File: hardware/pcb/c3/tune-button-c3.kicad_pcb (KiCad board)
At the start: 2 copper layers, 46 x 69.5 mm, 40 parts, among them J1 USB-C, J2 LiPo, Q1 AO3401A, SW1 MX switch, SW2 MX switch, SW3 MX switch, SW4 MX switch, SW5 RESET, SW6 BOOT, U1 ESP32-C3-WROOM-02-N4, U2 SRV05-4, U3 TP4054, U4 RT9080-3.3

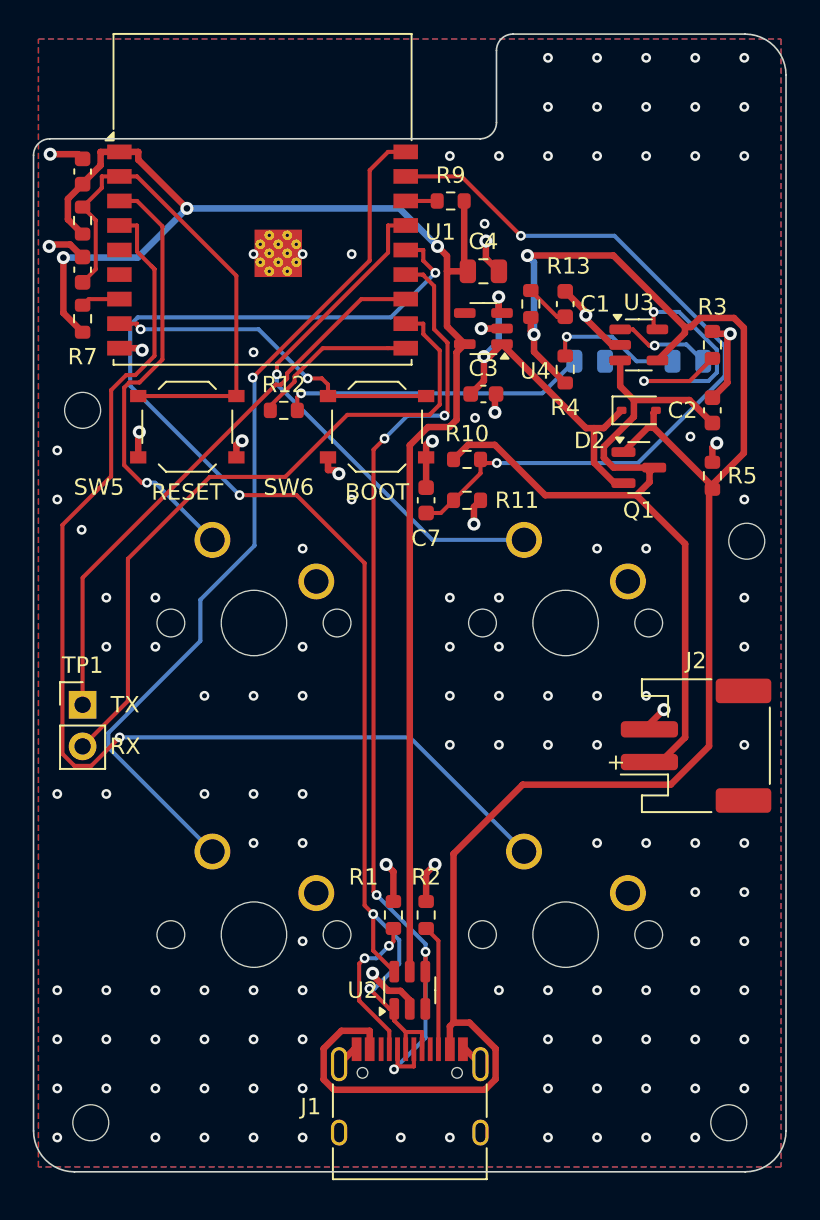
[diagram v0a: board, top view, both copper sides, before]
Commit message: pcb: fixes from the second DFM audit and visual review
- JLC BOM: no designator ranges (KiCad wrote R5-R7, so the CPL lost R5/R6/R7); fab_jlc.py now
  refuses a BOM part with no placement.
- Stitching vias kept off SMD pad openings (two were in the module ground pad's paste).
- Logo drawn as rows at the stroke pitch with caps inset, so gaps keep their size; 15 mm wide.
- Labels only where their own part is the nearest body (R13 and U4 were ambiguous).
- Battery + marks off the pads; USB-C slot paste overprinted 0.2 mm; footprint silk >= 0.15 mm.
- C3 board 70.1 mm long so the USB-C legs clear the switch housings by 0.3 mm.
- Stop tracking __pycache__.
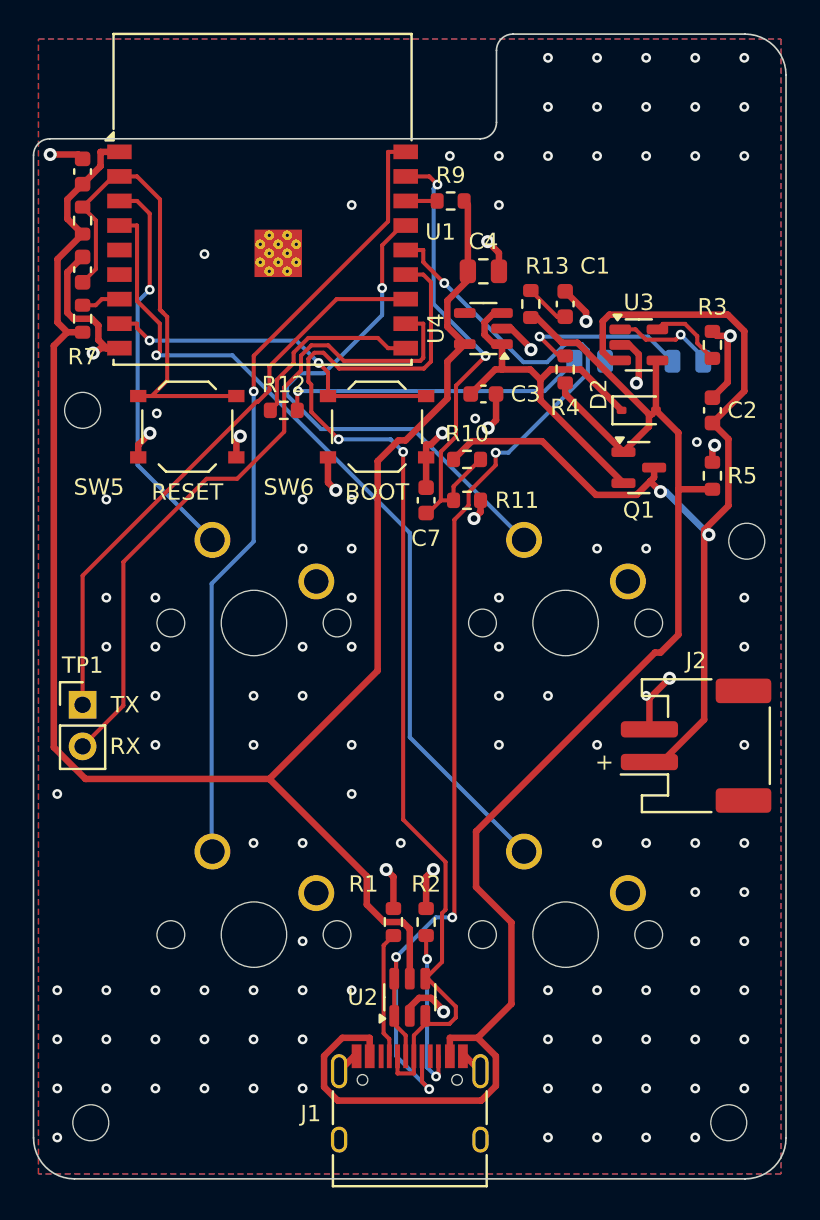
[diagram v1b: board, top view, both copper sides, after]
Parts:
- moved J1 0.43 mm to (23.0, 66.5)
- moved R1 0.43 mm to (22.0, 54.3)
- moved R2 0.43 mm to (24.0, 54.3)
- moved U2 0.43 mm to (23.0, 58.9)
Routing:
- net VBUS: track 116.0 -> 93.7 mm, vias 2 -> 0
- net VBAT_SENSE: track 48.0 -> 29.2 mm
- net K3: track 68.9 -> 52.1 mm
- net 3V3: track 96.2 -> 112.9 mm, vias 3 -> 0
- net VBAT: track 49.4 -> 62.8 mm, vias 0 -> 2
- net PROG: track 16.8 -> 4.63 mm, vias 2 -> 0
- net GND: track 44.8 -> 56.6 mm, vias 135 -> 124
- net USB_DP: track 84.0 -> 75.5 mm, vias 4 -> 5
- net USB_DN: track 62.5 -> 69.6 mm, vias 5 -> 2
- net K4: track 53.6 -> 48.3 mm
- net CHG_A: track 8.30 -> 10.8 mm
- net CC2: track 7.69 -> 10.2 mm, vias 0 -> 2
- net K2: track 26.5 -> 24.3 mm
- net CC1: track 9.45 -> 7.77 mm, vias 2 -> 0
- net EN: track 31.7 -> 30.2 mm
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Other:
- board size 46 x 69.5 mm -> 46 x 70 mm

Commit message: pcb (c3): fixes from the second simulation pass
- C1 4.7u -> 10u 0805 (C15850, Basic): with R13, plug-in ringing on low-resistance cables peaks
  around 5.6 V instead of 6.1 V (RT9080 absolute max 6.5 V).
- D4, a 1N5819WS across Q1: in the ~3-5 ms after unplugging, before Q1 turns on, the cell feeds
  VSYS through 0.35 V rather than the body diode's 0.6 V, so a Wi-Fi burst there stays above
  brown-out at a 3.4 V cell.
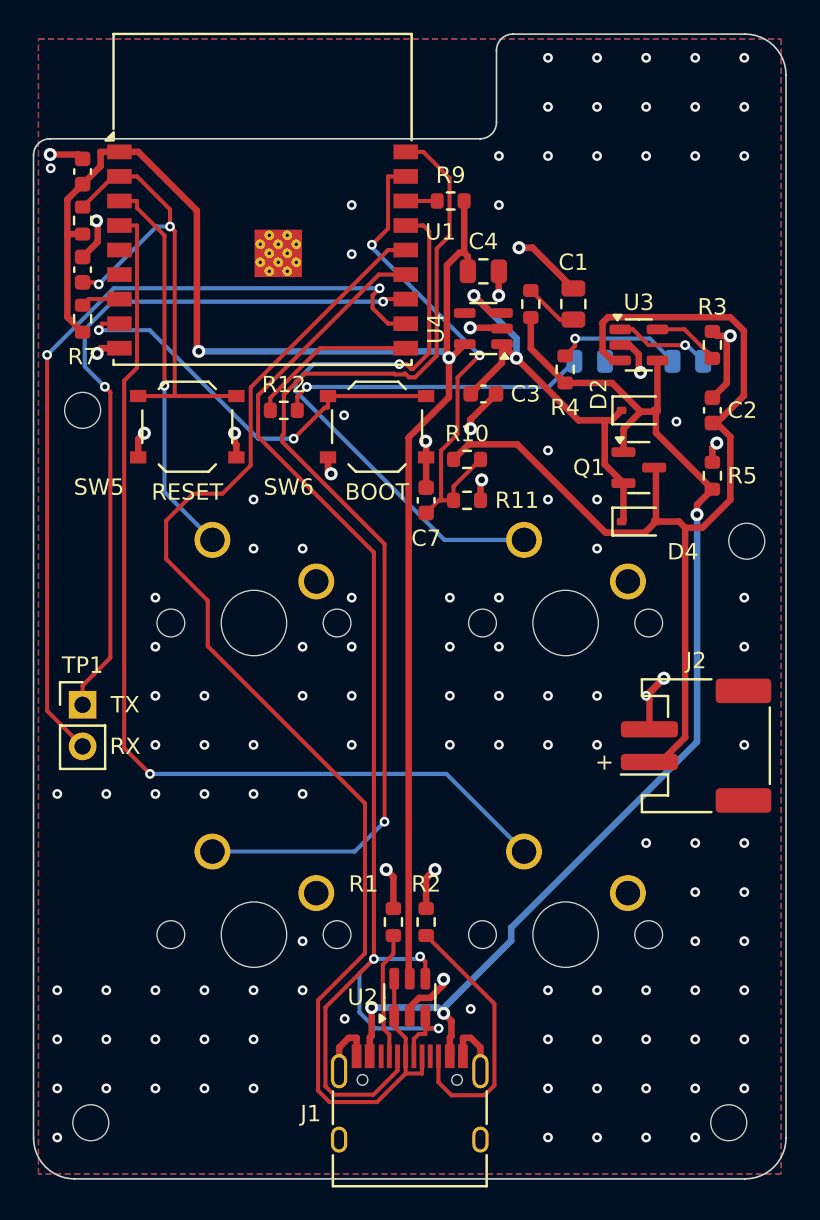
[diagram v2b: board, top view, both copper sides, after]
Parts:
- added D4: 1N5819WS, Diode_SMD:D_SOD-323, F.Cu at (37.0, 29.8)
- C1: value 4.7u -> 10u; footprint Capacitor_SMD:C_0603_1608Metric -> Capacitor_SMD:C_0805_2012Metric
- moved C1 0.50 mm to (33.0, 16.5)
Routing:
- net VBUS: track 93.7 -> 72.6 mm, vias 0 -> 3
- net K4: track 48.3 -> 65.1 mm
- net 3V3: track 112.9 -> 96.5 mm, vias 0 -> 2
- net USB_DN: track 69.6 -> 81.8 mm, vias 2 -> 3
- net TXD: track 35.5 -> 44.7 mm, vias 0 -> 2
- net RXD: track 41.9 -> 50.6 mm, vias 0 -> 2
- net K3: track 52.1 -> 60.4 mm
- net CC2: track 10.2 -> 16.5 mm, vias 2 -> 0
- net GND: track 56.6 -> 62.2 mm, vias 124 -> 129
- net USB_DP: track 75.5 -> 79.9 mm, vias 5 -> 0
- net IO9: track 21.6 -> 25.8 mm
- net K1: track 32.5 -> 36.4 mm
- net CHG_A: track 10.8 -> 7.84 mm
- net VSYS: track 24.7 -> 27.1 mm, vias 0 -> 2
- net LED: track 11.6 -> 10.3 mm
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
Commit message: pcb: black solder mask, white legend in the board stackup
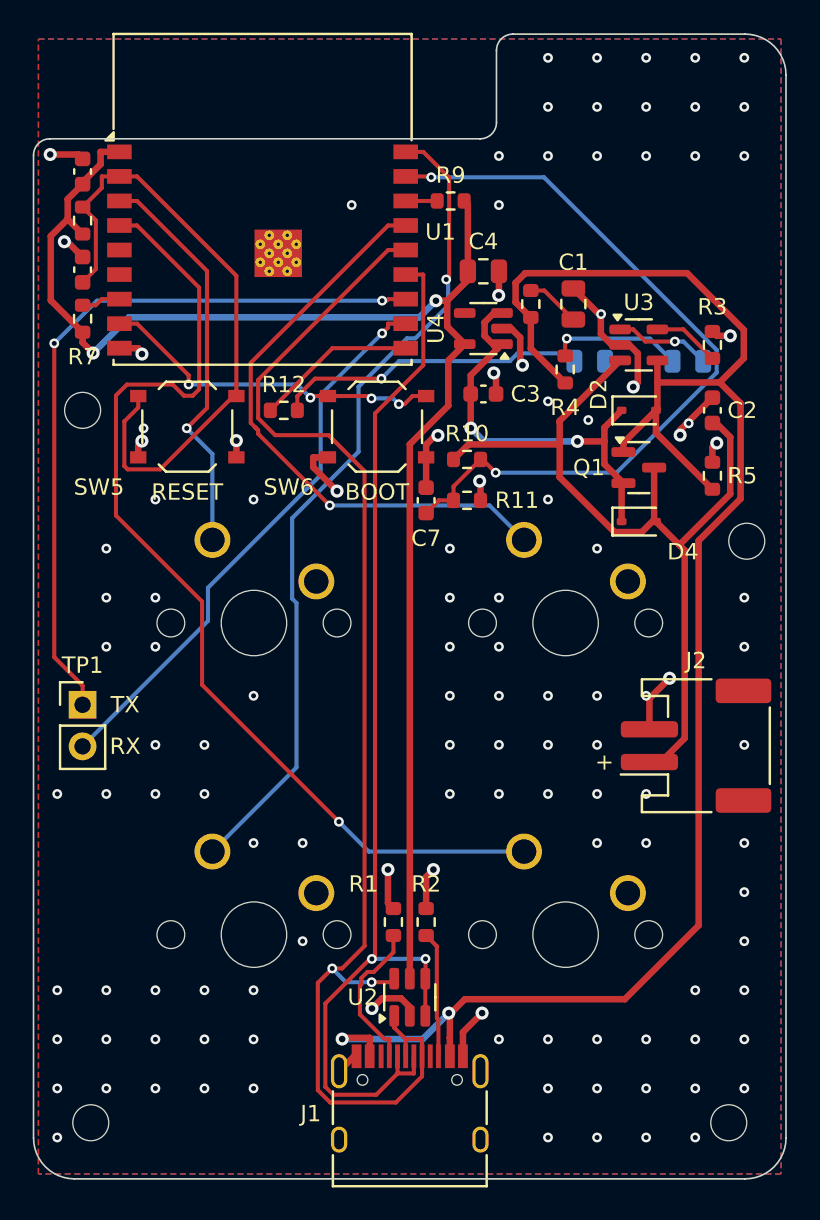
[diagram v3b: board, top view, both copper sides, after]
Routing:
- net VBUS: track 72.6 -> 108.5 mm, vias 3 -> 2
- net VBAT_SENSE: track 30.2 -> 47.3 mm
- net RXD: track 50.6 -> 34.7 mm, vias 2 -> 1
- net K4: track 65.1 -> 51.1 mm
- net USB_DN: track 81.8 -> 68.3 mm, vias 3 -> 2
- net VBAT: track 63.4 -> 52.4 mm
- net GND: track 62.2 -> 52.7 mm, vias 129 -> 122
- net CC2: track 16.5 -> 7.69 mm
- net EN: track 31.3 -> 39.4 mm, vias 2 -> 0
- net 3V3: track 96.5 -> 90.0 mm
- net IO9: track 25.8 -> 21.4 mm, vias 2 -> 4
- net K3: track 60.4 -> 62.2 mm
- net VSYS: track 27.1 -> 25.4 mm
- net CC1: track 7.81 -> 9.38 mm
- net K2: track 23.7 -> 24.7 mm
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
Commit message: pcb: third DFM audit and visual fixes
- JLCJLCJLCJLC order-number marker (C3 electronics side, XIAO back); README: black mask,
  lead-free HASL, 'Specify a location', overhang remark.
- Logo scaled by the mark's own extent (15 mm printed, was 12.4); vias 1 mm clear of back art.
- D1/D3 labels merged into the back text; keycaps are label obstacles on front-key boards.
- USB-C slot paste overprint 0.12 mm (0.15 mm stencil web).
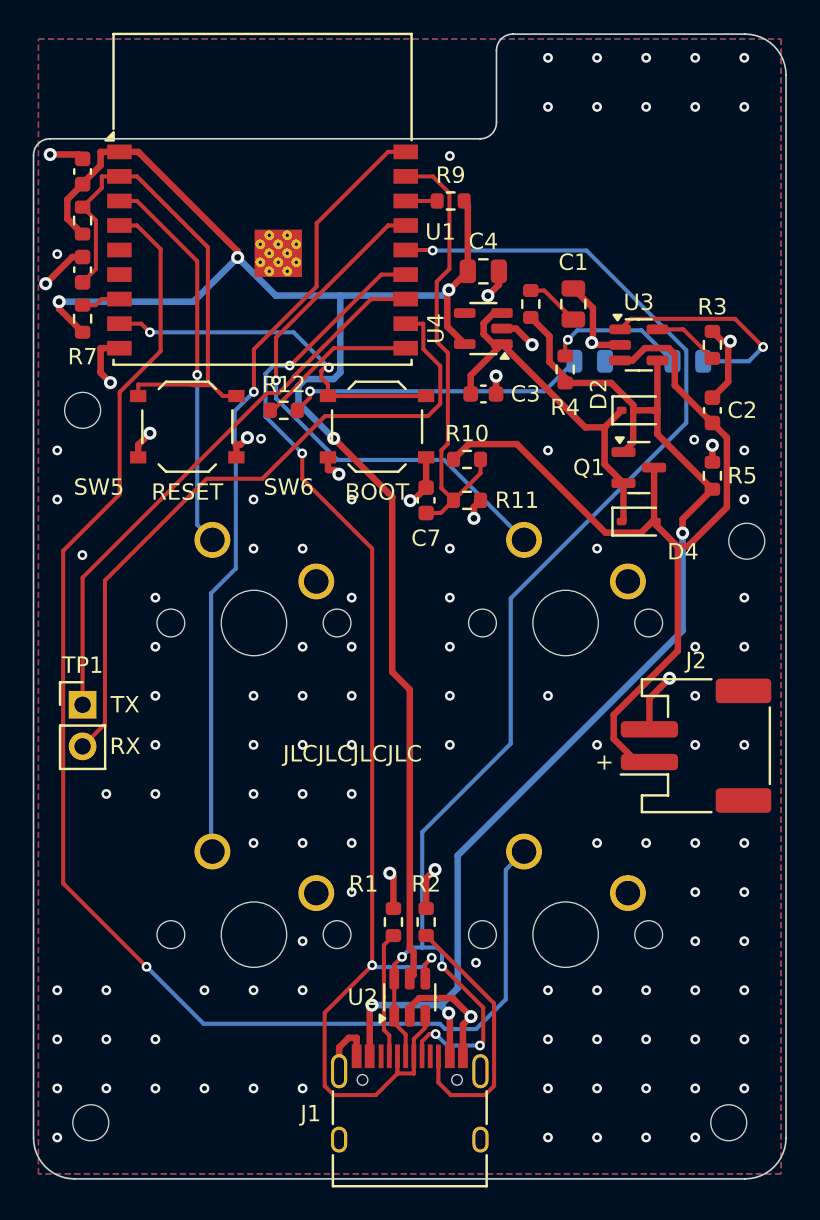
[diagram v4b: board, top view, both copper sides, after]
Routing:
- net VBUS: track 108.5 -> 72.8 mm, vias 2 -> 3
- net K3: track 62.2 -> 85.4 mm
- net VBAT_SENSE: track 47.3 -> 28.1 mm, vias 2 -> 0
- net 3V3: track 90.0 -> 102.7 mm, vias 2 -> 4
- net TXD: track 45.4 -> 34.6 mm, vias 2 -> 0
- net CC2: track 7.69 -> 16.5 mm
- net EN: track 39.4 -> 31.3 mm
- net STAT: track 5.88 -> 13.7 mm
- net RXD: track 34.7 -> 42.1 mm, vias 1 -> 0
- net USB_DN: track 68.3 -> 75.0 mm, vias 2 -> 4
- net USB_DP: track 79.5 -> 84.0 mm, vias 2 -> 5
- net VBAT: track 52.4 -> 55.3 mm
- net K1: track 36.7 -> 33.9 mm
- net K4: track 51.1 -> 48.4 mm
- net GND: track 52.7 -> 55.4 mm
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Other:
- board text added: "D1 CHG"
- board text added: "D3 LED"
- board text added: "JLCJLCJLCJLC"
- board text removed: "CHG"
- board text removed: "LED"

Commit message: pcb (c3): fixes from the third simulation pass
- C1's damping resistor 1 -> 0.5 ohm (R13 + R14, two Basic 1 ohm): with 1 ohm a stiff 5.5 V
  source and no cell rang VSYS to 6.8 V, past the RT9080's 6.5 V; 0.47 ohm simulated under 6.4 V
  on every cable corner.
- R5 10k -> 3.3k: the bigger C1 had stretched the unplug gap to 13-28 ms; ~5-7 ms again.
- README: D4's hot reverse leakage means the cell's protection board is the overcharge backstop.
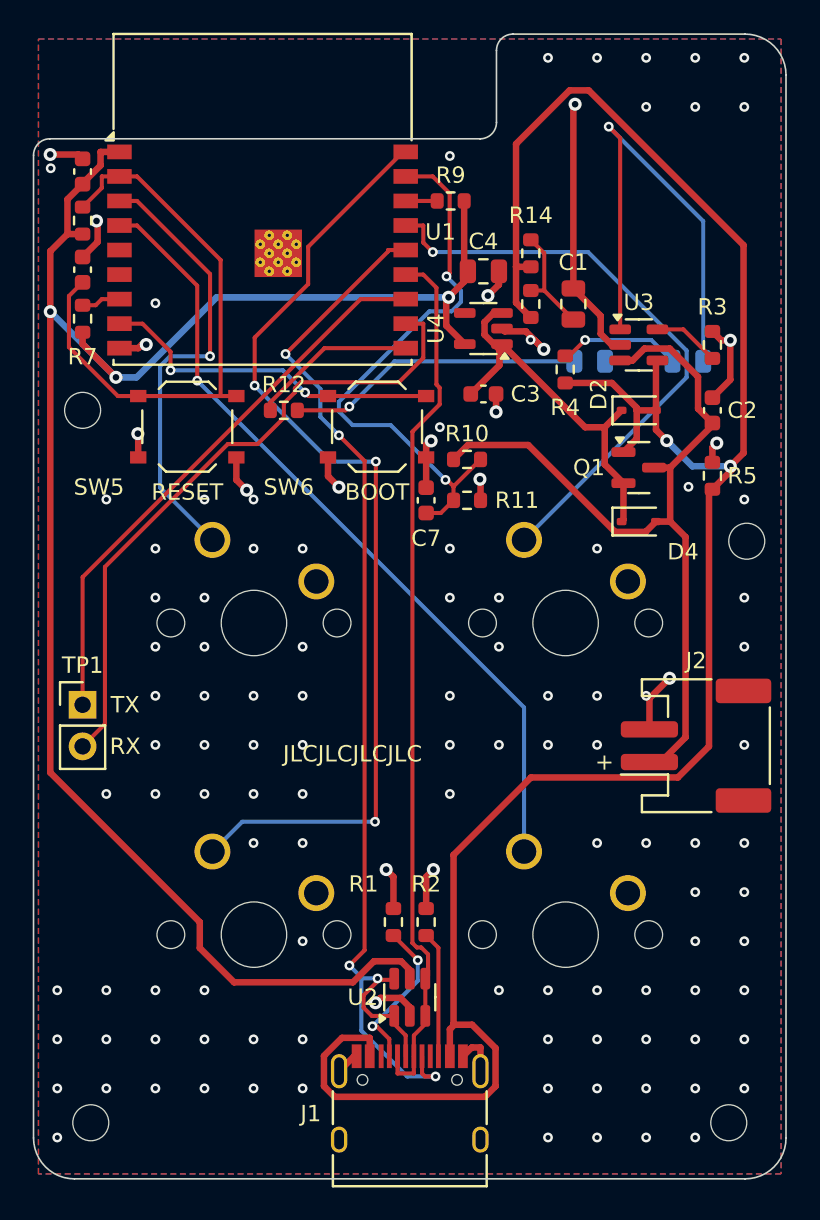
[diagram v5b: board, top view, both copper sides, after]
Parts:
- added R14: 1, Resistor_SMD:R_0603_1608Metric, F.Cu at (30.4, 13.4)
- R5: value 10k -> 3.3k
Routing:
- net VBUS: track 72.8 -> 135.2 mm, vias 3 -> 2
- net K3: track 85.4 -> 49.1 mm
- net USB_DN: track 75.0 -> 54.0 mm, vias 4 -> 0
- net STAT: track 13.7 -> 29.4 mm
- net USB_DP: track 84.0 -> 70.7 mm
- net K4: track 48.4 -> 60.3 mm, vias 1 -> 3
- net 3V3: track 102.7 -> 112.3 mm, vias 4 -> 3
- net CC2: track 16.5 -> 7.69 mm
- net GND: track 55.4 -> 63.7 mm
- net VBAT_SENSE: track 28.1 -> 34.9 mm, vias 0 -> 2
- net VBAT: track 55.3 -> 49.5 mm
- net EN: track 31.3 -> 35.8 mm
- net K2: track 23.7 -> 27.7 mm
- net VBUS_C: track 3.34 -> 6.78 mm
- net K1: track 33.9 -> 36.6 mm
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
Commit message: pcb: fourth DFM audit fixes
- route.py stitches with pour islands kept, then removes the ones still unconnected: a 44 mm2 pocket
  of back GND fenced in by tracks near the module was being dropped before it could get a via.
- Zero-length track segments pruned.
- Logo: gaps narrower than the 0.15 mm legend limit are opened to 0.15 rather than left to fill.
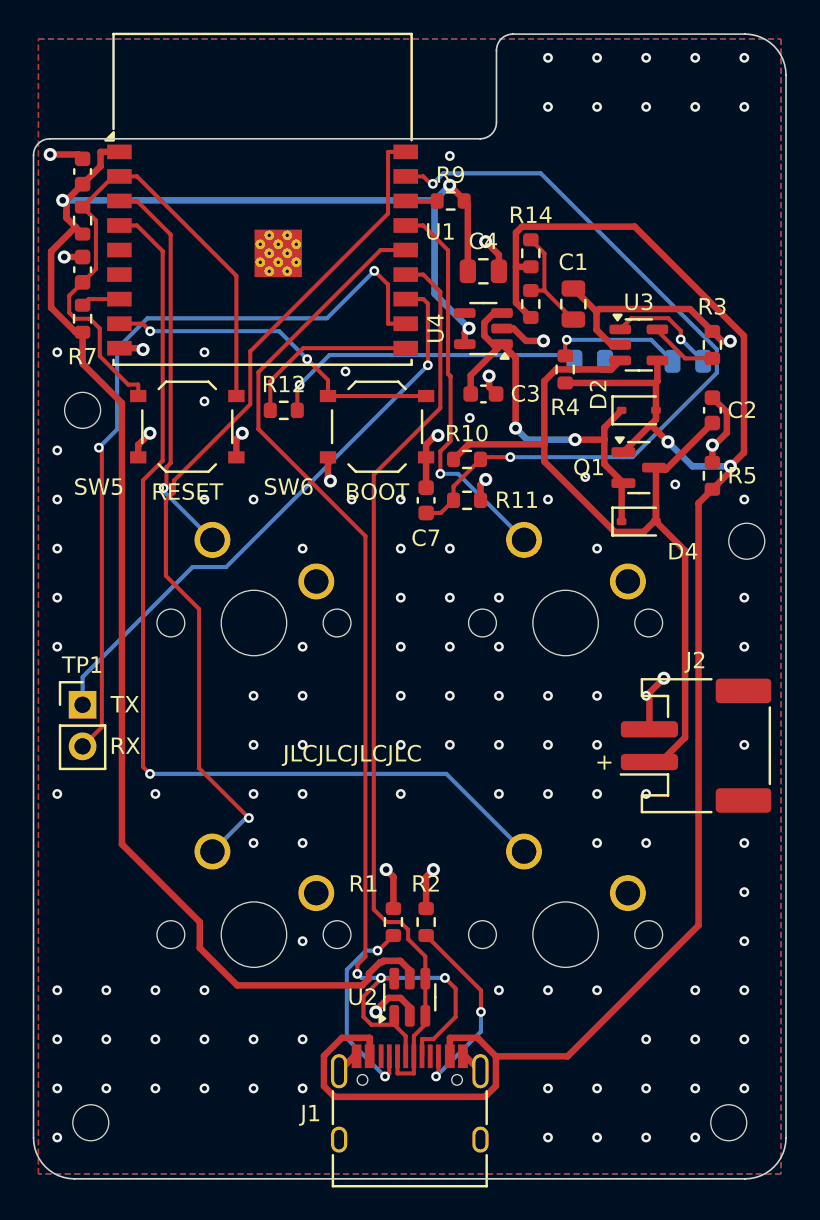
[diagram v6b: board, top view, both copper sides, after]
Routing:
- net STAT: track 29.4 -> 6.76 mm
- net VBUS: track 135.2 -> 117.6 mm
- net K1: track 36.6 -> 24.2 mm
- net VBAT_SENSE: track 34.9 -> 47.2 mm
- net K3: track 49.1 -> 60.8 mm
- net GND: track 63.7 -> 55.1 mm, vias 122 -> 126
- net K4: track 60.3 -> 52.6 mm, vias 3 -> 1
- net RXD: track 40.1 -> 47.7 mm, vias 0 -> 2
- net CC2: track 7.69 -> 12.4 mm, vias 0 -> 2
- net K2: track 27.7 -> 24.1 mm
- net CC1: track 9.72 -> 12.6 mm
- net VSYS: track 23.4 -> 26.1 mm, vias 0 -> 2
- net USB_DN: track 54.0 -> 56.4 mm
- net TXD: track 34.6 -> 35.9 mm, vias 0 -> 1
- net USB_DP: track 70.7 -> 72.0 mm, vias 5 -> 3
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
